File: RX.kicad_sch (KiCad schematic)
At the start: 22 parts, among them U9 LMK00304SQ_NOPB, Y1 ASE-50.000MHZ-LC-T

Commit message: almost finished, phew! just dd +/- 5v rails, connect the SDIO & power enable pins and figure out the rest of the clocking chain
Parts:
- removed R19: 10K, symbol Device:R_US
- added C108, C110, C111, C112, C115, C116, C117, C118, C119, C120, C122, C123, C124, C126, C127, C128: 1uF, symbol Device:C
- added C167, C168, C172, C173, C175, C176, C178, C179, C180, C215, C218: 100nF, symbol Device:C
- added C171, C174, C182: 10uF, symbol Device:C
- added R42, R57, R66, R67, R68, R70: 10K, symbol Device:R_US
- added R43: 0R, symbol Device:R_US
- added R69: 50R, symbol Device:R_US
- added U26: LMK00304SQ_NOPB, LMK00304SQ_NOPB:WQFN-32, symbol LMK00304SQ_NOPB:LMK00304SQ_NOPB
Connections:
- net +3V3 is gone; now on net FANOUT_VCC: C54.2, Y1.1 (TRI-STATE(STBY)), Y1.4 (VDD)
- net FANOUT_REFOUT_EN: now also R57.2
- net FANOUT_VCC: now also C167.2, C168.2, C171.2, R42.1, R57.1, R66.1, U26.10 (VCC), U26.2 (VCCOA), U26.28 (VCC_2), U26.5 (VCCOA_2)
- net FANOUT_VCCA: now also C172.2, C173.2, C174.2
- net FANOUT_VCCB: now also C176.2, C180.2, C182.2
- net GND: now also C108.2, C110.2, C111.2, C112.2, C115.2, C116.2, C117.2, C118.2, C119.2, C120.2, C122.2, C123.2, C124.2, C126.2, C127.2, C128.2, C167.1, C168.1, C171.1, C172.1, C173.1, C174.1, C176.1, C179.1, C180.1, C182.1, C215.1, C218.1, R67.2, R68.2, R69.1, R70.2, U26.1 (GND), U26.17 (GND3), U26.24 (GND4), U26.8 (GND2)
- net REF_CLK_OUT: now reaches U9.29 (REFOUT)
- net REF_CLK_OUT: now also R43.2
- net FANOUT_VCCC: now reaches U9.30 (VCCOUTC)
- net FANOUT_VCCC: now also C215.2, C218.2
- new net: C178.1, U26.14 (CLKIN0)
- new net: C179.2, U26.15 (CLKIN0_N)
- new net: C175.1, C178.2, R69.2
- new net: C175.2, R43.1
- new net AFE1_1V8A: C108.1
- new net AFE1_1V8D: C119.1
- new net AFE1_3V3A: C110.1
- new net AFE1_3V3D: C120.1
- new net AFE2_1V8A: C111.1
- new net AFE2_1V8D: C122.1
- new net AFE2_3V3A: C112.1
- new net AFE2_3V3D: C123.1
- new net AFE3_1V8A: C115.1
- new net AFE3_1V8D: C124.1
- new net AFE3_3V3A: C116.1
- new net AFE3_3V3D: C126.1
- new net AFE4_1V8A: C117.1
- new net AFE4_1V8D: C127.1
- new net AFE4_3V3A: C118.1
- new net AFE4_3V3D: C128.1
- new net SOM_SYNC_CLK_N: U26.7 (CLKOUTA1_N)
- new net SOM_SYNC_CLK_P: U26.6 (CLKOUTA1)
- new net SYNC_CLKIN_SEL0: R67.1, U26.13 (CLKIN_SEL0)
- new net SYNC_CLKIN_SEL1: R68.1, U26.16 (CLKIN_SEL1)
- new net SYNC_CLKOUT_TYPE0: R42.2, U26.9 (CLKOUT_TP0)
- new net SYNC_CLKOUT_TYPE1: R70.1, U26.32 (CLKOUT_TP1)
- new net SYNC_REFOUT_EN: R66.2, U26.31 (REFOUT_EN)
- new net TX_BF_CLK_N: U26.4 (CLKOUTA0_N)
- new net TX_BF_CLK_P: U26.3 (CLKOUTA0)
- no-connect marks 7 -> 18
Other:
- sheet RX_LANE renamed AFE1
- sheet RX_LANE1 renamed AFE2
- sheet RX_LANE2 renamed AFE3
- sheet RX_LANE3 renamed AFE4
- sheet AFE1 ports: added 1V8A, 1V8D, 3V3A, 3V3D; removed none
- sheet AFE2 ports: added 1V8A, 1V8D, 3V3A, 3V3D; removed none
- sheet AFE3 ports: added 1V8A, 1V8D, 3V3A, 3V3D; removed none
- sheet AFE4 ports: added 1V8A, 1V8D, 3V3A, 3V3D; removed none
- note added: "AFE IO are 3V3"
- moved on the sheet: C70, C74, C78, C79, C80, C81, C82, C86, C90

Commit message: DONE! hust needs a final revision, checking termination throughout the circuit and verifying the signal chain
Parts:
- removed C167, C168, C172, C173, C176, C180, C218, C74, C78, C79, C86, C90: 100nF, symbol Device:C
- removed C171, C174, C182, C80, C81, C82: 10uF, symbol Device:C
- removed R23, R27, R31, R35, R42, R57, R66, R67, R68, R70: 10K, symbol Device:R_US
- removed R43: 0R, symbol Device:R_US
- removed R69: 50R, symbol Device:R_US
- removed U26, U9: LMK00304SQ_NOPB, LMK00304SQ_NOPB:WQFN-32, symbol LMK00304SQ_NOPB:LMK00304SQ_NOPB
- removed Y1: ASE-50.000MHZ-LC-T, ASE-50.000MHZ-LC-T:XTAL_ASE-50.000MHZ-LC-T, symbol ASE-50.000MHZ-LC-T:ASE-50.000MHZ-LC-T
- added C235, C238: 10uF, symbol Device:C
- added C236, C237, C63: 100nF, symbol Device:C
- added U28, U29: LMK1D1204RGTR, VQFN16_RGT_TEX, symbol LMK1D1204RGTR:LMK1D1204RGTR
- added Y3: SG-8018CA_50.000000MHZ_TJHPB, SG-8018CA_50.000000MHZ_TJHPB:OSC_SG-8018CA_50.000000MHZ_TJHPB, symbol SG-8018CA_50.000000MHZ_TJHPB:SG-8018CA_50.000000MHZ_TJHPB
- C179, C215: value 100nF -> 10uF
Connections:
- net FANOUT_VCCC is gone; now on net CLK_1V8: C215.2
- net CLKOUT_A0_N: now also U29.10 (OUT0_N)
- net CLKOUT_A0_P: now also U29.9 (OUT0_P)
- net CLKOUT_A1_N: now also U29.12 (OUT1_N)
- net CLKOUT_A1_P: now also U29.11 (OUT1_P)
- net CLKOUT_B0_N: now also U29.14 (OUT2_N)
- net CLKOUT_B0_P: now also U29.13 (OUT2_P)
- net CLKOUT_B1_N: now also U29.16 (OUT3_N)
- net CLKOUT_B1_P: now also U29.15 (OUT3_P)
- net FANOUT_VCC: now also C235.2, C236.2, C237.2, C238.2, U29.2 (IN_SEL), U29.5 (VDD); no longer C54.2
- net GND: now also C175.1, C178.1, C235.1, C236.1, C237.1, C238.1, C63.1, U28.1 (GND), U28.17 (EPAD), U29.1 (GND), U29.17 (EPAD), Y3.2 (GND)
- net SOM_SYNC_CLK_N: now also U28.12 (OUT1_N)
- net SOM_SYNC_CLK_P: now also U28.11 (OUT1_P)
- net TX_BF_CLK_N: now also U28.10 (OUT0_N)
- net TX_BF_CLK_P: now also U28.9 (OUT0_P)
- net CLK_1V8: now reaches C179.2
- net CLK_1V8: now also C175.2, C178.2, C54.2, U28.2 (IN_SEL), U28.5 (VDD), Y3.1 (OE), Y3.4 (VCC)
- net at R15.2: now also Y3.3 (OUT)
- net at C62.1: now also U28.3 (IN1_P)
- net at C58.2: now also U28.4 (IN1_N)
- net FANOUT_VCCA renamed VAC_REF1
- net VAC_REF1: now also U29.8 (VAC_REF0)
- new net: U28.15 (OUT3_P), U29.3 (IN1_P)
- new net: U28.16 (OUT3_N), U29.4 (IN1_N)
- new net VAC_REF0: C63.2, U28.8 (VAC_REF0)
- no-connect marks 18 -> 6
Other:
- sheet AFE1 ports: added AFE_INA_P, AFE_INB_P, AFE_INC_P, AFE_IND_P; removed none
- sheet AFE2 ports: added AFE_INA_P, AFE_INB_P, AFE_INC_P, AFE_IND_P; removed none
- sheet AFE3 ports: added AFE_INA_P, AFE_INB_P, AFE_INC_P, AFE_IND_P; removed none
- sheet AFE4 ports: added AFE_INA_P, AFE_INB_P, AFE_INC_P, AFE_IND_P; removed none
- moved on the sheet: C108, C110, C111, C112, C115, C116, C117, C118, C119, C120, C122, C123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

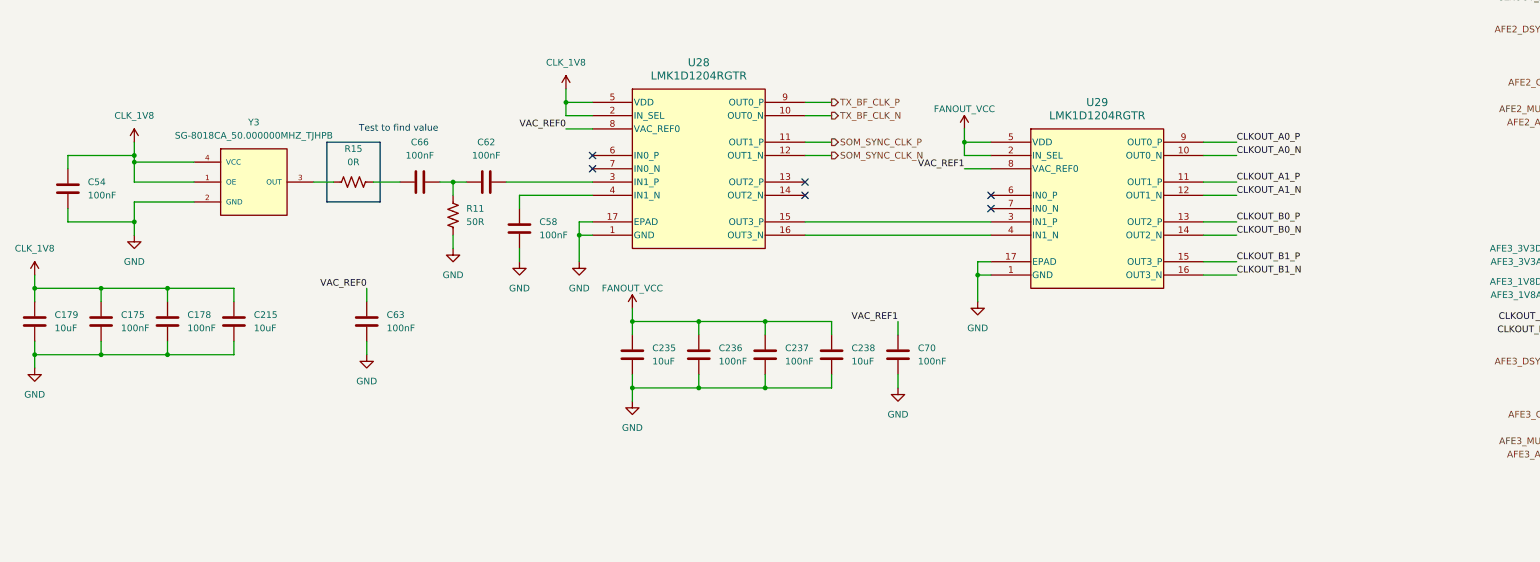
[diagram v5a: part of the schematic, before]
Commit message: HDMI was requested so add it and give the signal chain a final revision
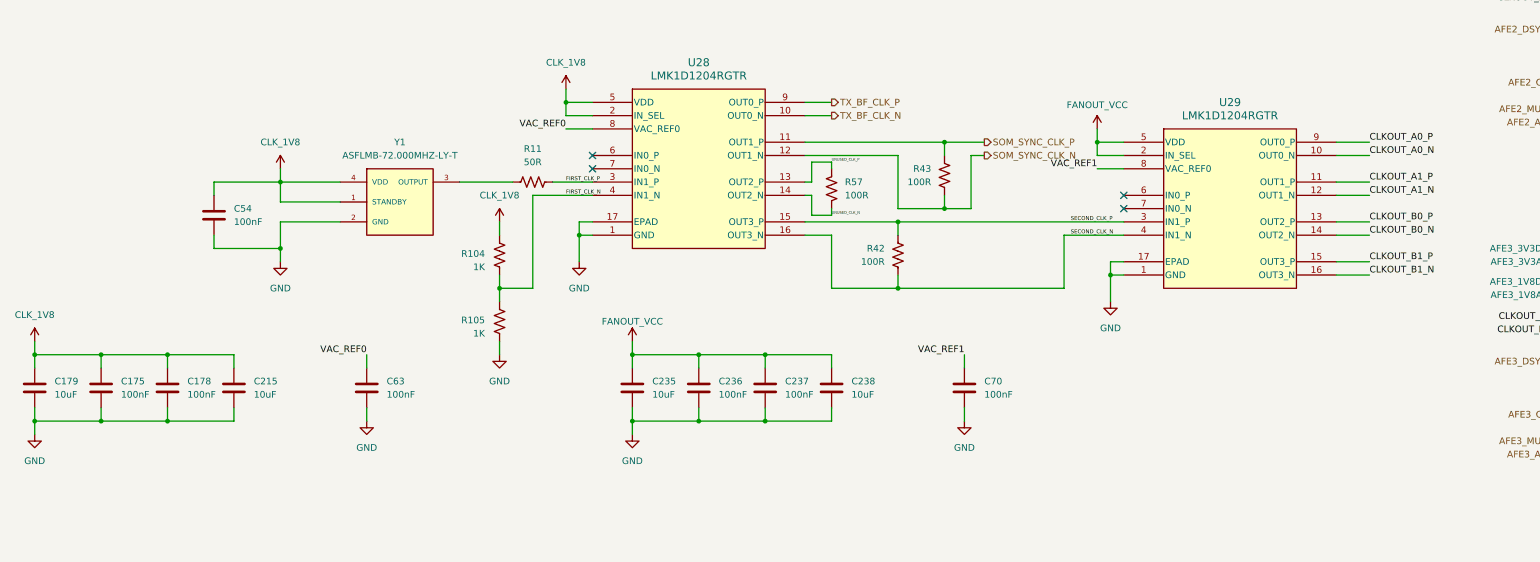
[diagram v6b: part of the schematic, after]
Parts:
- removed C58, C62, C66: 100nF, symbol Device:C
- removed R15: 0R, symbol Device:R_US
- removed Y3: SG-8018CA_50.000000MHZ_TJHPB, SG-8018CA_50.000000MHZ_TJHPB:OSC_SG-8018CA_50.000000MHZ_TJHPB, symbol SG-8018CA_50.000000MHZ_TJHPB:SG-8018CA_50.000000MHZ_TJHPB
- added R104, R105: 1K, symbol Device:R_US
- added R42, R43, R57: 100R, symbol Device:R_US
- added Y1: ASFLMB-72.000MHZ-LY-T, ASFLMB-72.000MHZ-LY-T:XTAL_ASFLMB-72.000MHZ-LY-T, symbol ASFLMB-72.000MHZ-LY-T:ASFLMB-72.000MHZ-LY-T
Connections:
- net CLK_1V8: now also R104.1, Y1.1 (STANDBY), Y1.4 (VDD)
- net GND: now also R105.2, Y1.2 (GND); no longer R11.1
- net SOM_SYNC_CLK_N: now also R43.2
- net SOM_SYNC_CLK_P: now also R43.1
- net UNUSED_CLK_P: now reaches U28.13 (OUT2_P)
- net UNUSED_CLK_P: now also R57.1
- net UNUSED_CLK_N: now reaches U28.14 (OUT2_N)
- net UNUSED_CLK_N: now also R57.2
- net SECOND_CLK_P: now reaches U28.15 (OUT3_P), U29.3 (IN1_P)
- net SECOND_CLK_P: now also R42.1
- net SECOND_CLK_N: now reaches U28.16 (OUT3_N), U29.4 (IN1_N)
- net SECOND_CLK_N: now also R42.2
- net FIRST_CLK_P: now reaches U28.3 (IN1_P)
- net FIRST_CLK_P: now also R11.1
- net FIRST_CLK_N: now reaches U28.4 (IN1_N)
- net FIRST_CLK_N: now also R104.2, R105.1
- net at R11.2: now also Y1.3 (OUTPUT)
- no-connect marks 6 -> 4
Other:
- note removed: "Test to find value"
- moved on the sheet: C175, C178, C179, C215, C235, C236, C237, C238, C54, C63, C70, R11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

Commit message: ALL IS DONE EXCEPT HDMI PLEASE HELP
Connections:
- net FANOUT_VCC renamed CLK_3V3
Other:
- note added: "72 MHz Crystal"
- note added: "Bias for common mode voltage (0.9v)"
- note added: "Fanout Buffer 1"
- note added: "Fanout Buffer 2"
- note added: "Feeds: 4 * AFE"
- note added: "Feeds: SOM sync signal Pulser beamformer sync signal AFE fanout buffer ->"
- note added: "It was recommended by the datasheet to terminate used & unused channels."
- note added: "Terminated at AFE side"
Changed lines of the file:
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@@
 	(generator_version "10.0")
 	(paper "A3")
+	(text "72 MHz Crystal"
+		(exclude_from_sim no)
+		(at 76.708 120.142 0)
+		(effects
+			(font
+				(size 3 3)
+				(thickness 0.6)
+				(bold yes)
+			)
+			(justify left)
+		)
+	)
 	(text "AFE IO are 3V3"
 		(exclude_from_sim no)
@@
 		)
 	)
+	(text "Fanout Buffer 2"
+		(exclude_from_sim no)
+		(at 237.49 103.378 0)
+		(effects
+			(font
+				(size 3 3)
+				(thickness 0.6)
+				(bold yes)
+			)
+			(justify left)
+		)
+	)
+	(text "Fanout Buffer 1\n"
+		(exclude_from_sim no)
+		(at 142.24 94.234 0)
+		(effects
+			(font
+				(size 3 3)
+				(thickness 0.6)
+				(bold yes)
+			)
+			(justify left)
+		)
+	)
+	(text "Terminated at AFE side"
+		(exclude_from_sim no)
+		(at 275.844 119.38 0)
+		(effects
+			(font
+				(size 1.27 1.27)
+				(thickness 0.254)
+				(bold yes)
+			)
+			(justify left)
+		)
+	)
+	(text "It was recommended by the datasheet to \nterminate used & unused channels."
+		(exclude_from_sim no)
+		(at 170.942 156.21 0)
+		(effects
+			(font
+				(size 1.27 1.27)
+			)
+			(justify left)
+		)
+	)
+	(text "Feeds:\nSOM sync signal\nPulser beamformer sync signal\nAFE fanout buffer ->"
+		(exclude_from_sim no)
+		(at 143.002 101.346 0)
+		(effects
+			(font
+				(size 1.27 1.27)
+				(thickness 0.1588)
+			)
+			(justify left)
+		)
+	)
+	(text "Bias for common mode voltage (0.9v)"
+		(exclude_from_sim no)
+		(at 75.438 154.94 0)
+		(effects
+			(font
+				(size 1.27 1.27)
+			)
+			(justify left)
+		)
+	)
+	(text "Feeds:\n4 * AFE"
+		(exclude_from_sim no)
+		(at 237.998 109.22 0)
+		(effects
+			(font
+				(size 1.27 1.27)
+				(thickness 0.1588)
+			)
+			(justify left)
+		)
+	)
 	(junction
 		(at 190.5 139.7)
@@
 	(wire
 		(pts
-			(xy 172.72 124.46) (xy 207.01 124.46)
+			(xy 172.72 124.46) (xy 205.74 124.46)
 		)
 		(stroke
@@
 	(wire
 		(pts
-			(xy 204.47 127) (xy 207.01 127)
+			(xy 204.47 127) (xy 205.74 127)
 		)
 		(stroke
@@
 	(wire
 		(pts
-			(xy 228.6 129.54) (xy 233.68 129.54)
+			(xy 231.14 129.54) (xy 233.68 129.54)
 		)
 		(stroke
@@
 	)
 	(label "VAC_REF1"
-		(at 228.6 129.54 180)
+		(at 231.14 129.54 180)
 		(effects
 			(font
@@
 	(hierarchical_label "SOM_SYNC_CLK_P"
 		(shape output)
-		(at 207.01 124.46 0)
+		(at 205.74 124.46 0)
 		(effects
 			(font
@@
 	(hierarchical_label "SOM_SYNC_CLK_N"
 		(shape output)
-		(at 207.01 127 0)
+		(at 205.74 127 0)
 		(effects
 			(font
@@
 			)
 		)
-		(property "Value" "FANOUT_VCC"
+		(property "Value" "CLK_3V3"
 			(at 139.7 158.75 0)
 			(show_name no)
@@
 			)
 		)
-		(property "Description" "Power symbol creates a global label with name \"FANOUT_VCC\""
+		(property "Description" "Power symbol creates a global label with name \"CLK_3V3\""
 			(at 139.7 162.56 0)
 			(hide yes)
@@
 	(symbol
 		(lib_id "power:VDD")
-		(at 228.6 121.92 0)
-		(unit 1)
-		(body_style 1)
-		(exclude_from_sim no)
-		(in_bom yes)
-		(on_board yes)
-		(in_pos_files yes)
-		(dnp no)
-		(property "Reference" "#PWR0329"
-			(at 228.6 125.73 0)
-			(hide yes)
-			(show_name no)
-			(do_not_autoplace no)
-			(effects
-				(font
-					(size 1.27 1.27)
-				)
-			)
-		)
-		(property "Value" "FANOUT_VCC"
-			(at 228.6 117.348 0)
-			(show_name no)
-			(do_not_autoplace no)
-			(effects
-				(font
-					(size 1.27 1.27)
-				)
-			)
-		)
-		(property "Footprint" ""
-			(at 228.6 121.92 0)
-			(hide yes)
-			(show_name no)
-			(do_not_autoplace no)
-			(effects
-				(font
-					(size 1.27 1.27)
-				)
-			)
-		)
-		(property "Datasheet" ""
-			(at 228.6 121.92 0)
-			(hide yes)
-			(show_name no)
-			(do_not_autoplace no)
-			(effects
-				(font
-					(size 1.27 1.27)
-				)
-			)
-		)
-		(property "Description" "Power symbol creates a global label with name \"FANOUT_VCC\""
-			(at 228.6 121.92 0)
-			(hide yes)
-			(show_name no)
-			(do_not_autoplace no)
-			(effects
-				(font
-					(size 1.27 1.27)
-				)
-			)
-		)
-		(pin "1"
-		)
-		(instances
-			(project "MedicalImager"
-				(path "/99848109-7be9-4113-bc9c-faf6c2acfe0b/ba161b84-3650-478e-81fe-b4f2d77a0043"
-					(reference "#PWR0329")
-					(unit 1)
-				)
-			)
-		)
-	)
-	(symbol
-		(lib_id "power:VDD")
 		(at 317.5 153.67 90)
 		(mirror x)
@@
 					(unit 1)
 				)
+			)
+		)
+	)
+	(symbol
+		(lib_id "power:VDD")
+		(at 228.6 121.92 0)
+		(unit 1)
+		(body_style 1)
+		(exclude_from_sim no)
+		(in_bom yes)
+		(on_board yes)
+		(in_pos_files yes)
+		(dnp no)
+		(property "Reference" "#PWR0343"
+			(at 228.6 125.73 0)
+			(hide yes)
+			(show_name no)
+			(do_not_autoplace no)
+			(effects
+				(font
+					(size 1.27 1.27)
+				)
+			)
+		)
+		(property "Value" "CLK_3V3"
+			(at 228.6 118.11 0)
+			(show_name no)
+			(do_not_autoplace no)
+			(effects
+				(font
+					(size 1.27 1.27)
+				)
+			)
+		)
+		(property "Footprint" ""
+			(at 228.6 121.92 0)
+			(hide yes)
+			(show_name no)
+			(do_not_autoplace no)
+			(effects
+				(font
+					(size 1.27 1.27)
+				)
+			)
+		)
+		(property "Datasheet" ""
+			(at 228.6 121.92 0)
+			(hide yes)
+			(show_name no)
+			(do_not_autoplace no)
+			(effects
+				(font
+					(size 1.27 1.27)
+				)
+			)
+		)
+		(property "Description" "Power symbol creates a global label with name \"CLK_3V3\""
+			(at 228.6 121.92 0)
+			(hide yes)
+			(show_name no)
+			(do_not_autoplace no)
+			(effects
+				(font
+					(size 1.27 1.27)
+				)
+			)
+		)
+		(pin "1"
+		)
+		(instances
+			(project "MedicalImager"
+				(path "/99848109-7be9-4113-bc9c-faf6c2acfe0b/ba161b84-3650-478e-81fe-b4f2d77a0043"
+					(reference "#PWR0343")
+					(unit 1)
+				)

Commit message: started layout, finished 90% of individual section placement, need to finish remaining and integrate together in PCB and apply schematic edits before
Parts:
- removed C108, C110, C111, C112, C115, C116, C117, C118: 1uF, symbol Device:C
- C301: renamed from C179; footprint (none) -> Capacitor_SMD:C_0402_1005Metric
- C302: renamed from C175; footprint (none) -> Capacitor_SMD:C_0402_1005Metric
- C303: renamed from C119; footprint (none) -> Capacitor_SMD:C_0402_1005Metric
- C305: renamed from C178; footprint (none) -> Capacitor_SMD:C_0402_1005Metric
- C306: renamed from C120; footprint (none) -> Capacitor_SMD:C_0402_1005Metric
- C308: renamed from C54; footprint (none) -> Capacitor_SMD:C_0402_1005Metric
- C309: renamed from C215; footprint (none) -> Capacitor_SMD:C_0402_1005Metric
- C310: renamed from C122; footprint (none) -> Capacitor_SMD:C_0402_1005Metric
- C312: renamed from C123; footprint (none) -> Capacitor_SMD:C_0402_1005Metric
- C314: renamed from C63; footprint (none) -> Capacitor_SMD:C_0402_1005Metric
- C315: renamed from C124; footprint (none) -> Capacitor_SMD:C_0402_1005Metric
- C317: renamed from C126; footprint (none) -> Capacitor_SMD:C_0402_1005Metric
- C319: renamed from C127; footprint (none) -> Capacitor_SMD:C_0402_1005Metric
- C321: renamed from C128; footprint (none) -> Capacitor_SMD:C_0402_1005Metric
- C323: renamed from C235; footprint (none) -> Capacitor_SMD:C_0402_1005Metric
- C324: renamed from C236; footprint (none) -> Capacitor_SMD:C_0402_1005Metric
- C325: renamed from C237; footprint (none) -> Capacitor_SMD:C_0402_1005Metric
- C326: renamed from C238; footprint (none) -> Capacitor_SMD:C_0402_1005Metric
- C327: renamed from C70; footprint (none) -> Capacitor_SMD:C_0402_1005Metric
- R301: renamed from R104; footprint (none) -> Resistor_SMD:R_0402_1005Metric
- R302: renamed from R105; footprint (none) -> Resistor_SMD:R_0402_1005Metric
- R303: renamed from R11; footprint (none) -> Resistor_SMD:R_0402_1005Metric
- R304: renamed from R57; footprint (none) -> Resistor_SMD:R_0402_1005Metric
- R305: renamed from R42; footprint (none) -> Resistor_SMD:R_0402_1005Metric
- R306: renamed from R43; footprint (none) -> Resistor_SMD:R_0402_1005Metric
- U301: renamed from U28; footprint VQFN16_RGT_TEX -> LMK1D1204RGTR:VQFN16_RGT_TEX
- U302: renamed from U29; footprint VQFN16_RGT_TEX -> LMK1D1204RGTR:VQFN16_RGT_TEX
- renumbered Y1 to Y301
